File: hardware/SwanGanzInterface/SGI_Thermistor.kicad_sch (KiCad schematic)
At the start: 20 parts, among them J3 Conn_01x03_Pin, U8 INA122D, U9 OPA2350

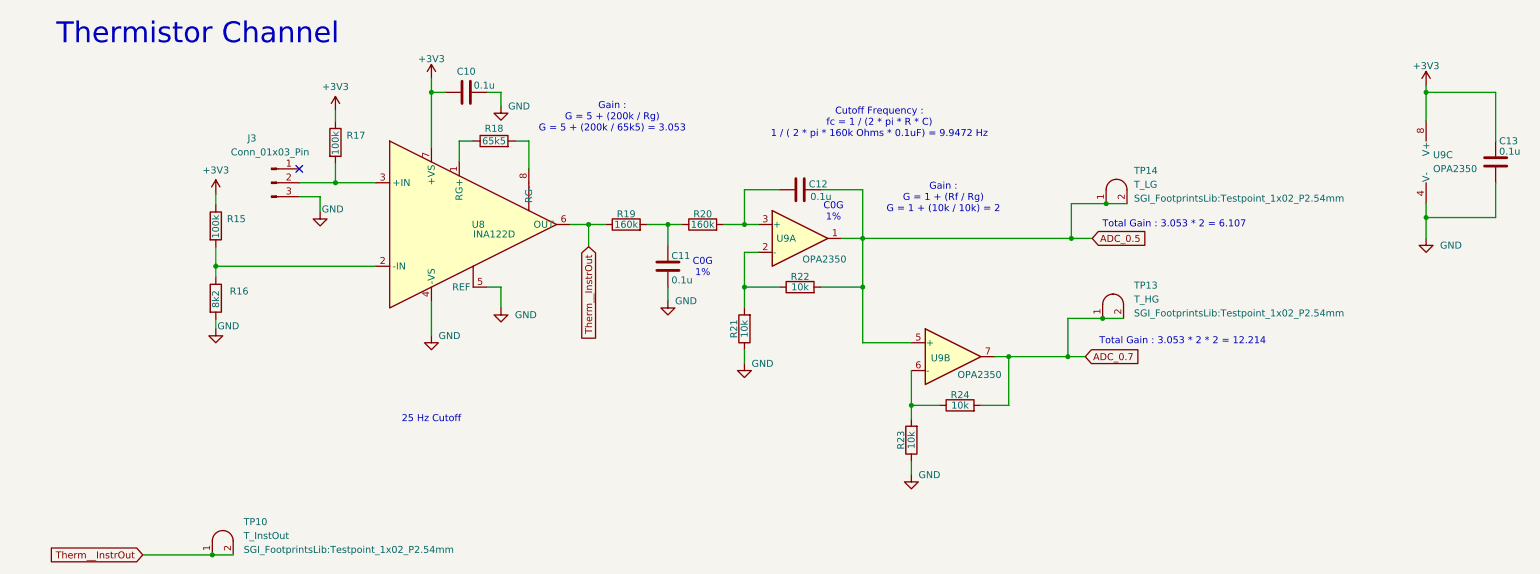
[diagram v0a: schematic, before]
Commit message: Reannotated symbols
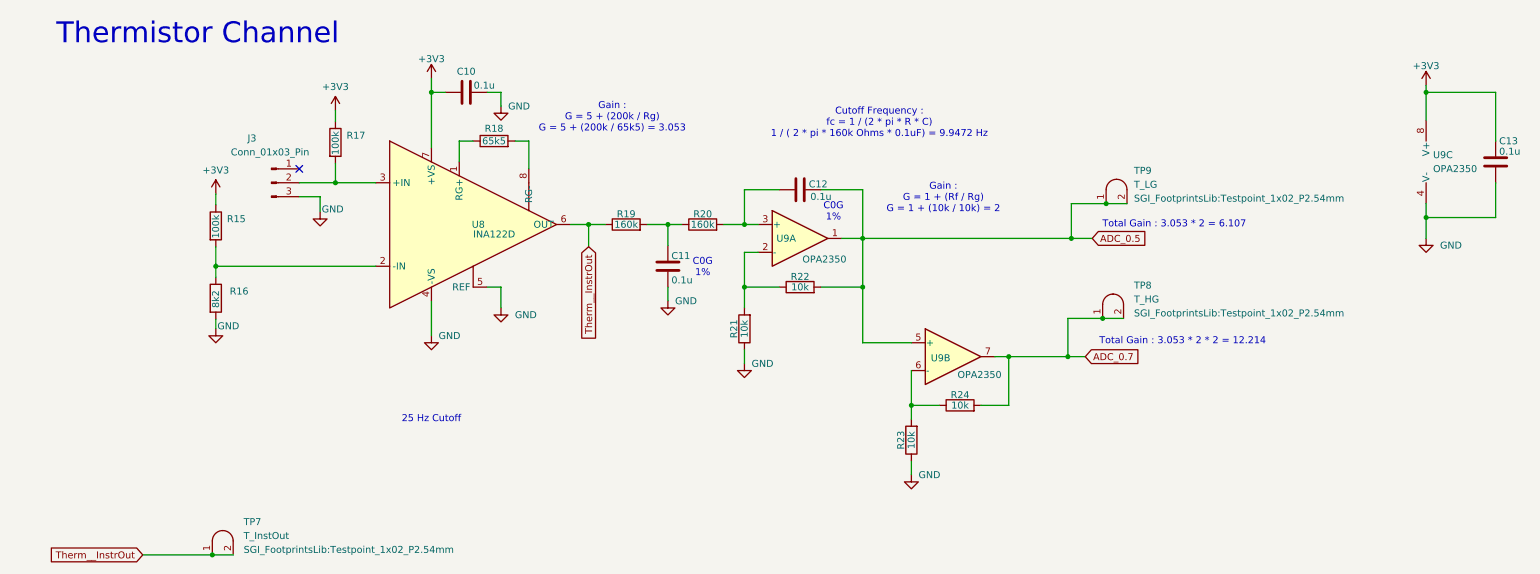
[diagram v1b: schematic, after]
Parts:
- renumbered TP10 to TP7, TP13 to TP8, TP14 to TP9
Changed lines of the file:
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@@
 		(on_board yes)
 		(dnp no)
-		(property "Reference" "#PWR048"
+		(property "Reference" "#PWR045"
 			(at 140.97 82.55 0)
 			(effects
@@
 			(project "SwanGanzInterface"
 				(path "/4e9a6e30-f660-472b-9696-bea1f34b4545/2d5e901e-83ed-4d76-b163-6429564a2d4c"
-					(reference "#PWR048")
+					(reference "#PWR045")
 					(unit 1)
 				)
@@
 		(on_board yes)
 		(dnp no)
-		(property "Reference" "#PWR045"
+		(property "Reference" "#PWR042"
 			(at 96.52 35.56 0)
 			(effects
@@
 			(project "SwanGanzInterface"
 				(path "/4e9a6e30-f660-472b-9696-bea1f34b4545/2d5e901e-83ed-4d76-b163-6429564a2d4c"
-					(reference "#PWR045")
+					(reference "#PWR042")
 					(unit 1)
 				)
@@
 		(dnp no)
 		(fields_autoplaced yes)
-		(property "Reference" "#PWR046"
+		(property "Reference" "#PWR043"
 			(at 96.52 72.39 0)
 			(effects
@@
 			(project "SwanGanzInterface"
 				(path "/4e9a6e30-f660-472b-9696-bea1f34b4545/2d5e901e-83ed-4d76-b163-6429564a2d4c"
-					(reference "#PWR046")
+					(reference "#PWR043")
 					(unit 1)
 				)
@@
 		(on_board yes)
 		(dnp no)
-		(property "Reference" "#PWR043"
+		(property "Reference" "#PWR040"
 			(at 83.82 27.94 0)
 			(effects
@@
 			(project "SwanGanzInterface"
 				(path "/4e9a6e30-f660-472b-9696-bea1f34b4545/2d5e901e-83ed-4d76-b163-6429564a2d4c"
-					(reference "#PWR043")
+					(reference "#PWR040")
 					(unit 1)
 				)
@@
 		(on_board yes)
 		(dnp no)
-		(property "Reference" "#PWR049"
+		(property "Reference" "#PWR046"
 			(at 171.45 102.87 0)
 			(effects
@@
 			(project "SwanGanzInterface"
 				(path "/4e9a6e30-f660-472b-9696-bea1f34b4545/2d5e901e-83ed-4d76-b163-6429564a2d4c"
-					(reference "#PWR049")
+					(reference "#PWR046")
 					(unit 1)
 				)
@@
 		(dnp no)
 		(fields_autoplaced yes)
-		(property "Reference" "#PWR039"
+		(property "Reference" "#PWR036"
 			(at 44.45 49.022 0)
 			(effects
@@
 			(project "SwanGanzInterface"
 				(path "/4e9a6e30-f660-472b-9696-bea1f34b4545/2d5e901e-83ed-4d76-b163-6429564a2d4c"
-					(reference "#PWR039")
+					(reference "#PWR036")
 					(unit 1)
 				)
@@
 		(dnp no)
 		(fields_autoplaced yes)
-		(property "Reference" "#PWR051"
+		(property "Reference" "#PWR048"
 			(at 265.43 59.69 0)
 			(effects
@@
 			(project "SwanGanzInterface"
 				(path "/4e9a6e30-f660-472b-9696-bea1f34b4545/2d5e901e-83ed-4d76-b163-6429564a2d4c"
-					(reference "#PWR051")
+					(reference "#PWR048")
 					(unit 1)
 				)
@@
 		(on_board yes)
 		(dnp no)
-		(property "Reference" "#PWR040"
+		(property "Reference" "#PWR037"
 			(at 44.45 76.2 0)
 			(effects
@@
 			(project "SwanGanzInterface"
 				(path "/4e9a6e30-f660-472b-9696-bea1f34b4545/2d5e901e-83ed-4d76-b163-6429564a2d4c"
-					(reference "#PWR040")
+					(reference "#PWR037")
 					(unit 1)
 				)
@@
 		(on_board yes)
 		(dnp no)
-		(property "Reference" "#PWR041"
+		(property "Reference" "#PWR038"
 			(at 63.5 54.864 0)
 			(effects
@@
 			(project ""
 				(path "/4e9a6e30-f660-472b-9696-bea1f34b4545/2d5e901e-83ed-4d76-b163-6429564a2d4c"
-					(reference "#PWR041")
+					(reference "#PWR038")
 					(unit 1)
 				)
@@
 		(dnp no)
 		(fields_autoplaced yes)
-		(property "Reference" "#PWR042"
+		(property "Reference" "#PWR039"
 			(at 66.294 33.782 0)
 			(effects
@@
 			(project ""
 				(path "/4e9a6e30-f660-472b-9696-bea1f34b4545/2d5e901e-83ed-4d76-b163-6429564a2d4c"
-					(reference "#PWR042")
+					(reference "#PWR039")
 					(unit 1)
 				)
@@
 		(on_board yes)
 		(dnp no)
-		(property "Reference" "#PWR050"
+		(property "Reference" "#PWR047"
 			(at 265.43 29.21 0)
 			(effects
@@
 			(project "SwanGanzInterface"
 				(path "/4e9a6e30-f660-472b-9696-bea1f34b4545/2d5e901e-83ed-4d76-b163-6429564a2d4c"
-					(reference "#PWR050")
+					(reference "#PWR047")
 					(unit 1)
 				)
@@
 		(dnp no)
 		(fields_autoplaced yes)
-		(property "Reference" "TP10"
+		(property "Reference" "TP7"
 			(at 49.53 105.0923 0)
 			(effects
@@
 			(project ""
 				(path "/4e9a6e30-f660-472b-9696-bea1f34b4545/2d5e901e-83ed-4d76-b163-6429564a2d4c"
-					(reference "TP10")
+					(reference "TP7")
 					(unit 1)
 				)
@@
 		(dnp no)
 		(fields_autoplaced yes)
-		(property "Reference" "TP14"
+		(property "Reference" "TP9"
 			(at 212.09 40.9573 0)
 			(effects
@@
 			(project "SwanGanzInterface"
 				(path "/4e9a6e30-f660-472b-9696-bea1f34b4545/2d5e901e-83ed-4d76-b163-6429564a2d4c"
-					(reference "TP14")
+					(reference "TP9")
 					(unit 1)
 				)
@@
 		(on_board yes)
 		(dnp no)
-		(property "Reference" "#PWR044"
+		(property "Reference" "#PWR041"
 			(at 83.82 77.47 0)
 			(effects
@@
 			(project "SwanGanzInterface"
 				(path "/4e9a6e30-f660-472b-9696-bea1f34b4545/2d5e901e-83ed-4d76-b163-6429564a2d4c"
-					(reference "#PWR044")
+					(reference "#PWR041")
 					(unit 1)
 				)
@@
 		(dnp no)
 		(fields_autoplaced yes)
-		(property "Reference" "TP13"
+		(property "Reference" "TP8"
 			(at 212.09 61.9123 0)
 			(effects
@@
 			(project "SwanGanzInterface"
 				(path "/4e9a6e30-f660-472b-9696-bea1f34b4545/2d5e901e-83ed-4d76-b163-6429564a2d4c"
-					(reference "TP13")
+					(reference "TP8")
 					(unit 1)
 				)
@@
 		(on_board yes)
 		(dnp no)
-		(property "Reference" "#PWR047"
+		(property "Reference" "#PWR044"
 			(at 127 71.12 0)
 			(effects
@@
 			(project "SwanGanzInterface"
 				(path "/4e9a6e30-f660-472b-9696-bea1f34b4545/2d5e901e-83ed-4d76-b163-6429564a2d4c"
-					(reference "#PWR047")
-					(unit 1)
-				)
+					(reference "#PWR044")
+					(unit 1)
+				)

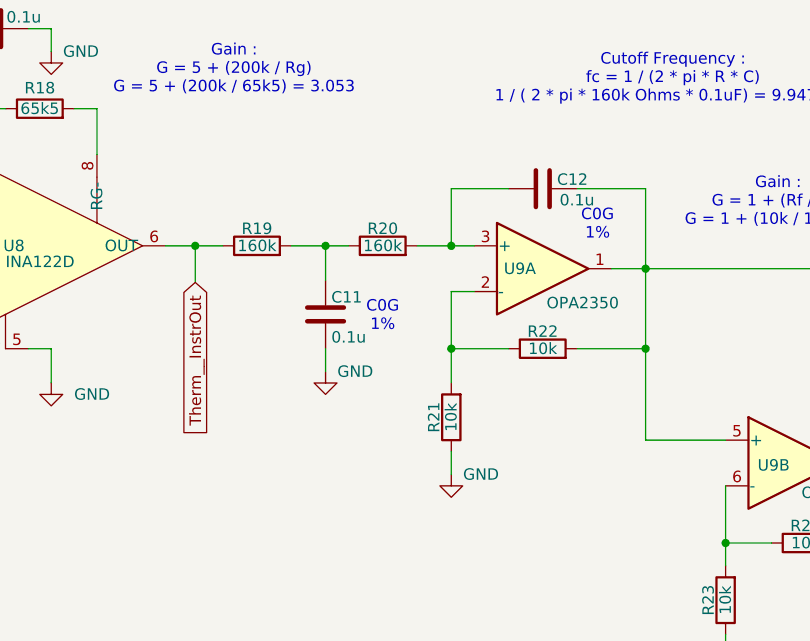
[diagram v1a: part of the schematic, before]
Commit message: Fixed butterworth filters
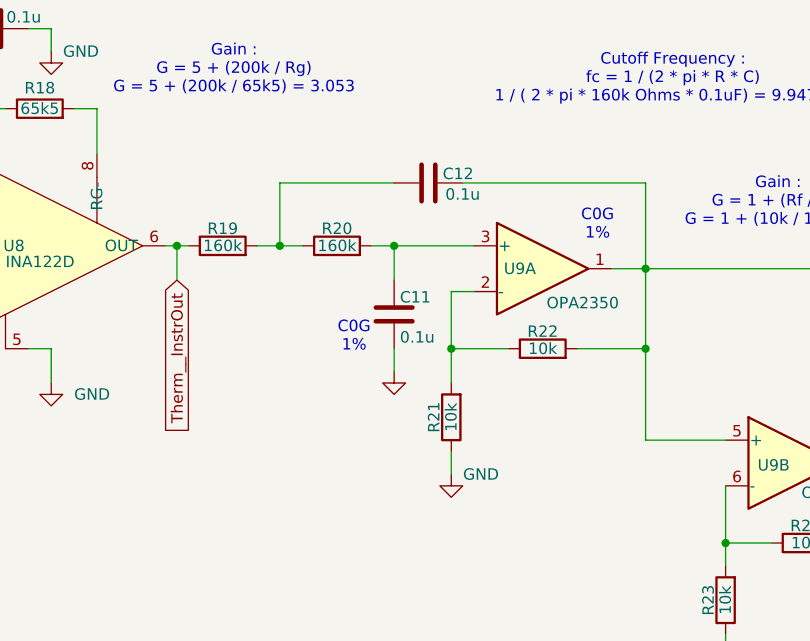
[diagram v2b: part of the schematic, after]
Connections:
- net at R20.2, U9.3 (+): now also C11.1; no longer C12.1
- net at R19.2, R20.1: now also C12.1; no longer C11.1
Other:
- moved on the sheet: C11, C12, R19, R20

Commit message: Driver Power
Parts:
- renumbered R15 to R14, R16 to R15, R17 to R16, R18 to R17, R19 to R18, R20 to R19, R21 to R20, R22 to R21, R23 to R22, R24 to R23
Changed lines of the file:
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@@
 		(on_board yes)
 		(dnp no)
-		(property "Reference" "#PWR045"
+		(property "Reference" "#PWR044"
 			(at 140.97 82.55 0)
 			(effects
@@
 			(project "SwanGanzInterface"
 				(path "/4e9a6e30-f660-472b-9696-bea1f34b4545/2d5e901e-83ed-4d76-b163-6429564a2d4c"
-					(reference "#PWR045")
+					(reference "#PWR044")
 					(unit 1)
 				)
@@
 		(on_board yes)
 		(dnp no)
-		(property "Reference" "R15"
+		(property "Reference" "R14"
 			(at 46.482 49.7839 0)
 			(effects
@@
 			(project "SwanGanzInterface"
 				(path "/4e9a6e30-f660-472b-9696-bea1f34b4545/2d5e901e-83ed-4d76-b163-6429564a2d4c"
-					(reference "R15")
+					(reference "R14")
 					(unit 1)
 				)
@@
 		(on_board yes)
 		(dnp no)
-		(property "Reference" "#PWR042"
+		(property "Reference" "#PWR041"
 			(at 96.52 35.56 0)
 			(effects
@@
 			(project "SwanGanzInterface"
 				(path "/4e9a6e30-f660-472b-9696-bea1f34b4545/2d5e901e-83ed-4d76-b163-6429564a2d4c"
-					(reference "#PWR042")
+					(reference "#PWR041")
 					(unit 1)
 				)
@@
 		(dnp no)
 		(fields_autoplaced yes)
-		(property "Reference" "#PWR043"
+		(property "Reference" "#PWR042"
 			(at 96.52 72.39 0)
 			(effects
@@
 			(project "SwanGanzInterface"
 				(path "/4e9a6e30-f660-472b-9696-bea1f34b4545/2d5e901e-83ed-4d76-b163-6429564a2d4c"
-					(reference "#PWR043")
+					(reference "#PWR042")
 					(unit 1)
 				)
@@
 		(on_board yes)
 		(dnp no)
-		(property "Reference" "#PWR040"
+		(property "Reference" "#PWR039"
 			(at 83.82 27.94 0)
 			(effects
@@
 			(project "SwanGanzInterface"
 				(path "/4e9a6e30-f660-472b-9696-bea1f34b4545/2d5e901e-83ed-4d76-b163-6429564a2d4c"
-					(reference "#PWR040")
+					(reference "#PWR039")
 					(unit 1)
 				)
@@
 		(on_board yes)
 		(dnp no)
-		(property "Reference" "#PWR046"
+		(property "Reference" "#PWR045"
 			(at 171.45 102.87 0)
 			(effects
@@
 			(project "SwanGanzInterface"
 				(path "/4e9a6e30-f660-472b-9696-bea1f34b4545/2d5e901e-83ed-4d76-b163-6429564a2d4c"
-					(reference "#PWR046")
+					(reference "#PWR045")
 					(unit 1)
 				)
@@
 		(dnp no)
 		(fields_autoplaced yes)
-		(property "Reference" "#PWR036"
+		(property "Reference" "#PWR035"
 			(at 44.45 49.022 0)
 			(effects
@@
 			(project "SwanGanzInterface"
 				(path "/4e9a6e30-f660-472b-9696-bea1f34b4545/2d5e901e-83ed-4d76-b163-6429564a2d4c"
-					(reference "#PWR036")
+					(reference "#PWR035")
 					(unit 1)
 				)
@@
 		(on_board yes)
 		(dnp no)
-		(property "Reference" "R17"
+		(property "Reference" "R16"
 			(at 68.326 34.5439 0)
 			(effects
@@
 			(project ""
 				(path "/4e9a6e30-f660-472b-9696-bea1f34b4545/2d5e901e-83ed-4d76-b163-6429564a2d4c"
-					(reference "R17")
+					(reference "R16")
 					(unit 1)
 				)
@@
 		(on_board yes)
 		(dnp no)
-		(property "Reference" "R21"
+		(property "Reference" "R20"
 			(at 139.065 69.85 90)
 			(effects
@@
 			(project "SwanGanzInterface"
 				(path "/4e9a6e30-f660-472b-9696-bea1f34b4545/2d5e901e-83ed-4d76-b163-6429564a2d4c"
-					(reference "R21")
+					(reference "R20")
 					(unit 1)
 				)
@@
 		(on_board yes)
 		(dnp no)
-		(property "Reference" "R22"
+		(property "Reference" "R21"
 			(at 151.13 60.325 90)
 			(effects
@@
 			(project "SwanGanzInterface"
 				(path "/4e9a6e30-f660-472b-9696-bea1f34b4545/2d5e901e-83ed-4d76-b163-6429564a2d4c"
-					(reference "R22")
+					(reference "R21")
 					(unit 1)
 				)
@@
 		(on_board yes)
 		(dnp no)
-		(property "Reference" "R19"
+		(property "Reference" "R18"
 			(at 115.57 48.895 90)
 			(effects
@@
 			(project ""
 				(path "/4e9a6e30-f660-472b-9696-bea1f34b4545/2d5e901e-83ed-4d76-b163-6429564a2d4c"
-					(reference "R19")
+					(reference "R18")
 					(unit 1)
 				)
@@
 		(dnp no)
 		(fields_autoplaced yes)
-		(property "Reference" "#PWR048"
+		(property "Reference" "#PWR047"
 			(at 265.43 59.69 0)
 			(effects
@@
 			(project "SwanGanzInterface"
 				(path "/4e9a6e30-f660-472b-9696-bea1f34b4545/2d5e901e-83ed-4d76-b163-6429564a2d4c"
-					(reference "#PWR048")
+					(reference "#PWR047")
 					(unit 1)
 				)
@@
 		(on_board yes)
 		(dnp no)
-		(property "Reference" "R24"
+		(property "Reference" "R23"
 			(at 180.34 81.915 90)
 			(effects
@@
 			(project "SwanGanzInterface"
 				(path "/4e9a6e30-f660-472b-9696-bea1f34b4545/2d5e901e-83ed-4d76-b163-6429564a2d4c"
-					(reference "R24")
+					(reference "R23")
 					(unit 1)
 				)
@@
 		(on_board yes)
 		(dnp no)
-		(property "Reference" "R20"
+		(property "Reference" "R19"
 			(at 128.27 48.895 90)
 			(effects
@@
 			(project ""
 				(path "/4e9a6e30-f660-472b-9696-bea1f34b4545/2d5e901e-83ed-4d76-b163-6429564a2d4c"
-					(reference "R20")
+					(reference "R19")
 					(unit 1)
 				)
@@
 		(on_board yes)
 		(dnp no)
-		(property "Reference" "R16"
+		(property "Reference" "R15"
 			(at 46.99 62.9919 0)
 			(effects
@@
 			(project ""
 				(path "/4e9a6e30-f660-472b-9696-bea1f34b4545/2d5e901e-83ed-4d76-b163-6429564a2d4c"
-					(reference "R16")
+					(reference "R15")
 					(unit 1)
 				)
@@
 		(on_board yes)
 		(dnp no)
-		(property "Reference" "#PWR037"
+		(property "Reference" "#PWR036"
 			(at 44.45 76.2 0)
 			(effects
@@
 			(project "SwanGanzInterface"
 				(path "/4e9a6e30-f660-472b-9696-bea1f34b4545/2d5e901e-83ed-4d76-b163-6429564a2d4c"
-					(reference "#PWR037")
+					(reference "#PWR036")
 					(unit 1)
 				)
@@
 		(on_board yes)
 		(dnp no)
-		(property "Reference" "#PWR038"
+		(property "Reference" "#PWR037"
 			(at 63.5 54.864 0)
 			(effects
@@
 			(project ""
 				(path "/4e9a6e30-f660-472b-9696-bea1f34b4545/2d5e901e-83ed-4d76-b163-6429564a2d4c"
-					(reference "#PWR038")
+					(reference "#PWR037")
 					(unit 1)
 				)
@@
 		(dnp no)
 		(fields_autoplaced yes)
-		(property "Reference" "#PWR039"
+		(property "Reference" "#PWR038"
 			(at 66.294 33.782 0)
 			(effects
@@
 			(project ""
 				(path "/4e9a6e30-f660-472b-9696-bea1f34b4545/2d5e901e-83ed-4d76-b163-6429564a2d4c"
-					(reference "#PWR039")
+					(reference "#PWR038")
 					(unit 1)
 				)
@@
 		(on_board yes)
 		(dnp no)
-		(property "Reference" "#PWR047"
+		(property "Reference" "#PWR046"
 			(at 265.43 29.21 0)
 			(effects
@@
 			(project "SwanGanzInterface"
 				(path "/4e9a6e30-f660-472b-9696-bea1f34b4545/2d5e901e-83ed-4d76-b163-6429564a2d4c"
-					(reference "#PWR047")
+					(reference "#PWR046")
 					(unit 1)
 				)
@@
 		(on_board yes)
 		(dnp no)
-		(property "Reference" "R18"
+		(property "Reference" "R17"
 			(at 95.25 33.274 90)
 			(effects
@@
 			(project ""
 				(path "/4e9a6e30-f660-472b-9696-bea1f34b4545/2d5e901e-83ed-4d76-b163-6429564a2d4c"
-					(reference "R18")
+					(reference "R17")
 					(unit 1)
 				)
@@
 		(on_board yes)
 		(dnp no)
-		(property "Reference" "#PWR041"
+		(property "Reference" "#PWR040"
 			(at 83.82 77.47 0)
 			(effects
@@
 			(project "SwanGanzInterface"
 				(path "/4e9a6e30-f660-472b-9696-bea1f34b4545/2d5e901e-83ed-4d76-b163-6429564a2d4c"
-					(reference "#PWR041")
+					(reference "#PWR040")
 					(unit 1)
 				)
@@
 		(on_board yes)
 		(dnp no)
-		(property "Reference" "R23"
+		(property "Reference" "R22"
 			(at 169.545 90.17 90)
 			(effects
@@
 			(project "SwanGanzInterface"
 				(path "/4e9a6e30-f660-472b-9696-bea1f34b4545/2d5e901e-83ed-4d76-b163-6429564a2d4c"
-					(reference "R23")
+					(reference "R22")
 					(unit 1)
 				)
@@
 		(on_board yes)
 		(dnp no)
-		(property "Reference" "#PWR044"
+		(property "Reference" "#PWR043"
 			(at 134.62 71.12 0)
 			(effects
@@
 			(project "SwanGanzInterface"
 				(path "/4e9a6e30-f660-472b-9696-bea1f34b4545/2d5e901e-83ed-4d76-b163-6429564a2d4c"
-					(reference "#PWR044")
-					(unit 1)
-				)
+					(reference "#PWR043")
+					(unit 1)
+				)
